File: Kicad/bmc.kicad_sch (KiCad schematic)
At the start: 30 parts, among them J1601 Header, J1602 Header, J1603 Conn_01x05, J1604 Double-mini-DIN-6, SW1601 SW_DIP_x01, SW1602 SW_DIP_x01, U1601 STM32F031K6T6

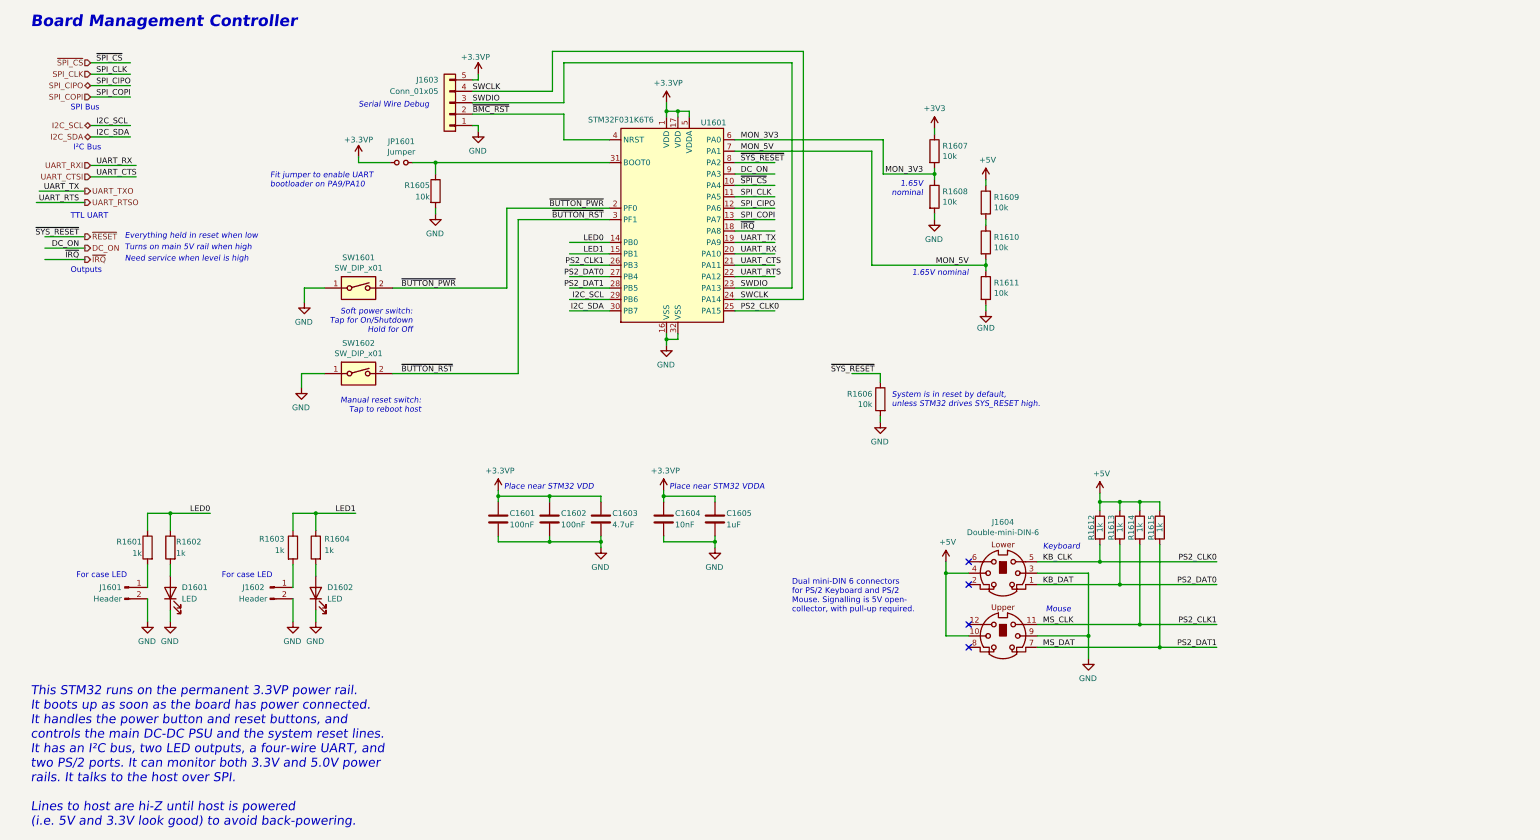
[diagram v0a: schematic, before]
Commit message: Update schematic files to Kicad 6.
Had to fix some symbols which didn't have perfect matches in K6.
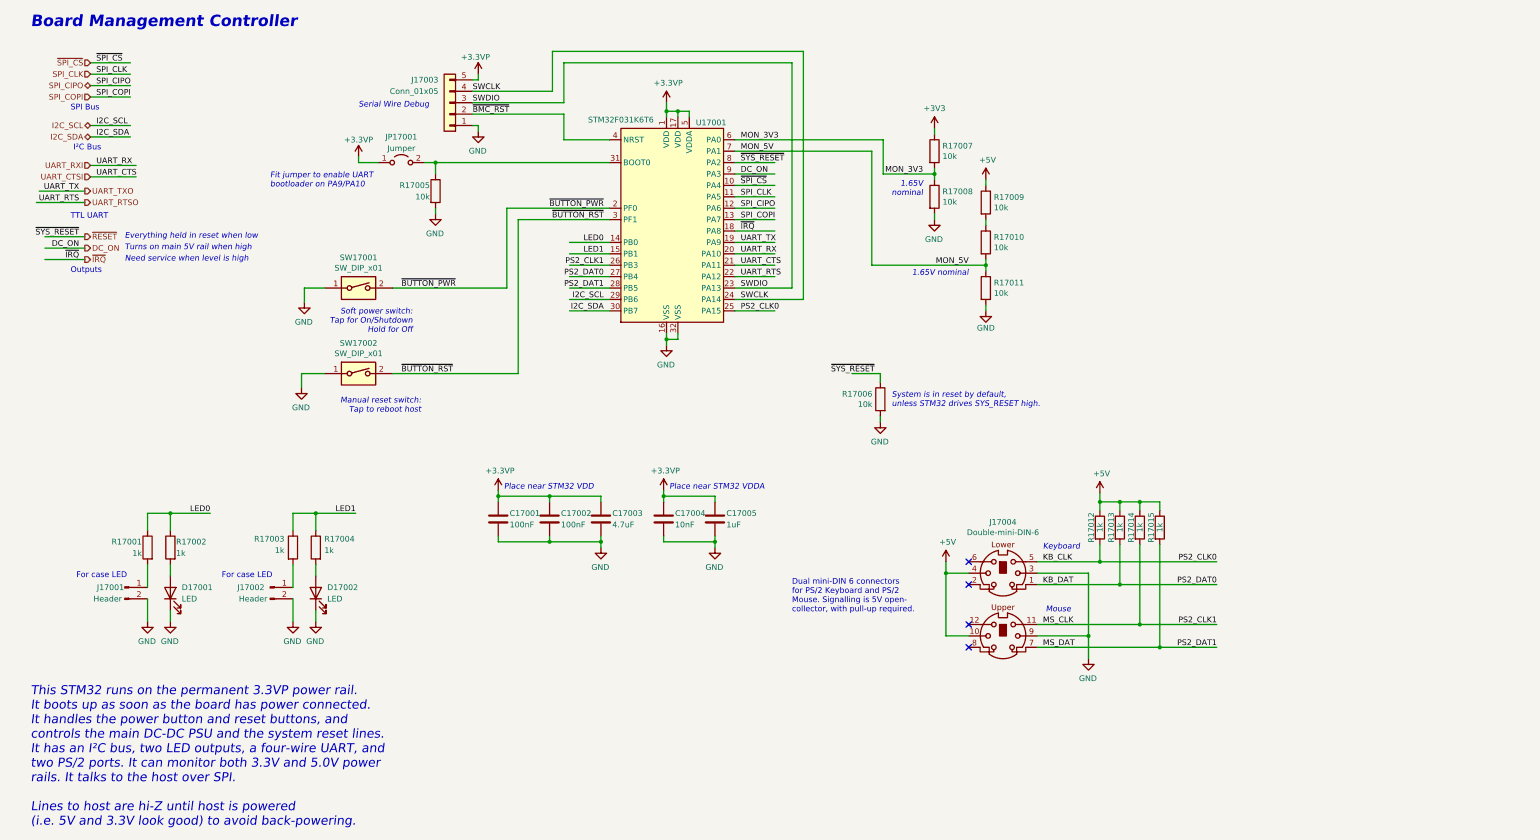
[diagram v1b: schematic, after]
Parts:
- JP17001: renamed from JP1601; symbol Neotron-Common-Hardware-rescue:Jumper_NO_Small-Device -> Jumper:Jumper_2_Open
- renumbered C1601 to C17001, C1602 to C17002, C1603 to C17003, C1604 to C17004, C1605 to C17005, D1601 to D17001, D1602 to D17002, J1601 to J17001, J1602 to J17002, J1603 to J17003, J1604 to J17004, R1601 to R17001, R1602 to R17002, R1603 to R17003, R1604 to R17004, R1605 to R17005, R1606 to R17006, R1607 to R17007, R1608 to R17008, R1609 to R17009, R1610 to R17010, R1611 to R17011, R1612 to R17012, R1613 to R17013, R1614 to R17014, R1615 to R17015, SW1601 to SW17001, SW1602 to SW17002, U1601 to U17001

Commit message: Imported sheets from Neotron Pico.
Standardised on +3V3 not +3.3V
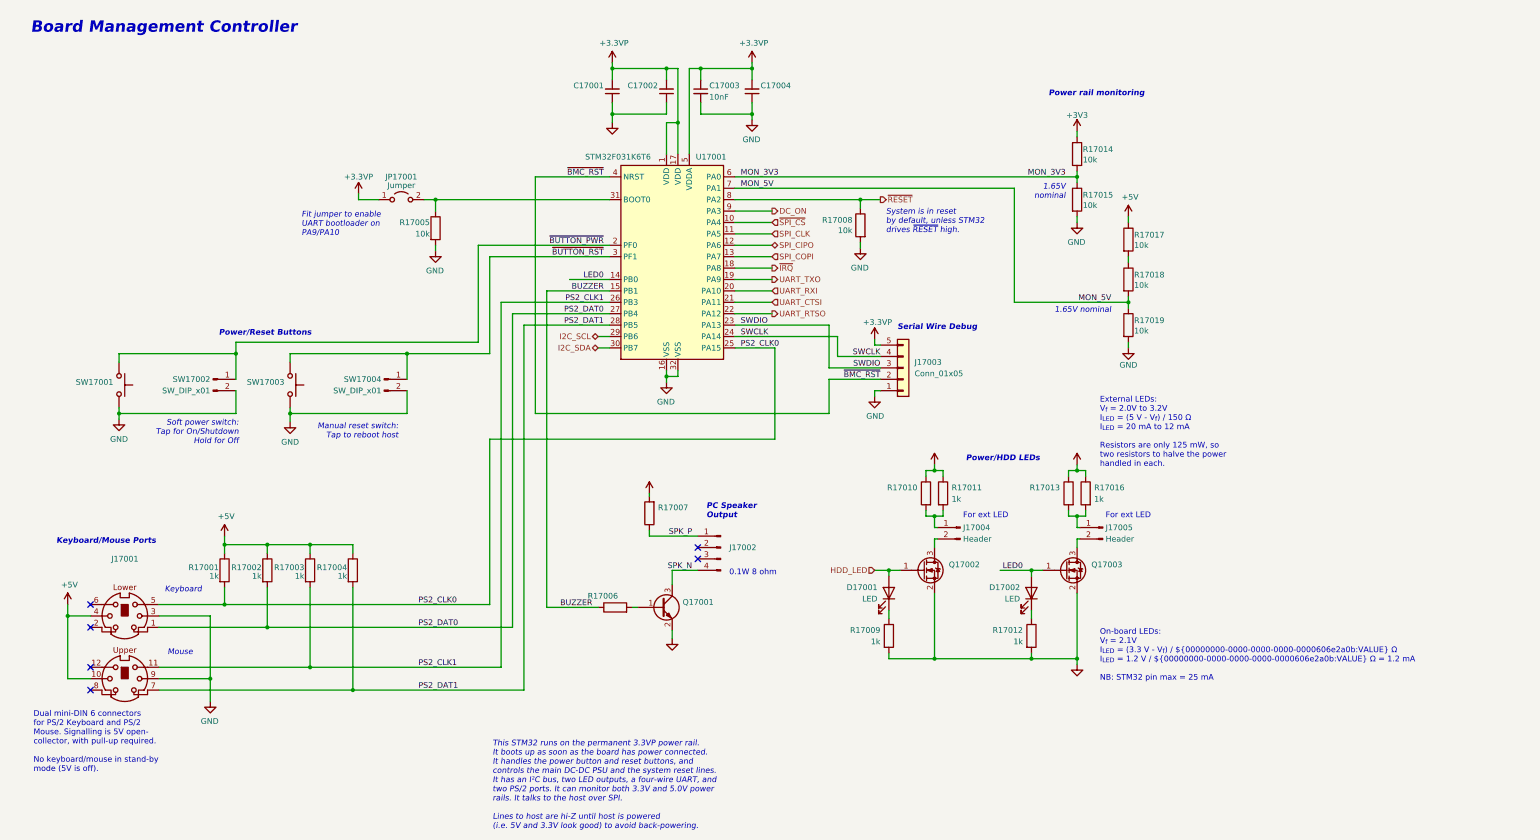
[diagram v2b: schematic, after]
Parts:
- removed C17001, C17002: 100nF, Capacitor_SMD:C_0805_2012Metric_Pad1.18x1.45mm_HandSolder, symbol Device:C
- removed C17003: 4.7uF, Capacitor_SMD:C_0805_2012Metric_Pad1.18x1.45mm_HandSolder, symbol Device:C
- removed C17005: 1uF, Capacitor_SMD:C_0805_2012Metric_Pad1.18x1.45mm_HandSolder, symbol Device:C
- removed J17004: Double-mini-DIN-6, Neotron-Common-Hardware:Double_mini-DIN_6, symbol Neotron-Common-Hardware:Double-mini-DIN-6
- added C17001, C17002, C17004: (no value), symbol Device:C_Small
- added J17001: (no value), symbol Neotron-Common-Hardware:Double-mini-DIN-6
- added J17002: (no value), symbol Connector:Conn_01x04_Male
- added Q17001: (no value), symbol Transistor_BJT:BC817
- added Q17002, Q17003: (no value), symbol Transistor_FET:2N7002
- added R17006, R17007, R17010, R17013: (no value), symbol Device:R
- added SW17001, SW17003: (no value), symbol Switch:SW_Push
- C17003: renamed from C17004; symbol Device:C -> Device:C_Small; Digikey 1276-1249-1-ND -> (none); JLCPCB Collection (none) -> Basic; Tolerance X5R -> X7R; Voltage 10V -> 50V
- D17001, D17002: JLCPCB Collection (none) -> Basic; LCSC Part# (none) -> C2296; MPN CPL-LED-3MM-RED -> 17-21SUYC/TR8; Manufacturer CPL -> Hubei KENTO; Voltage (none) -> 2.1V
- J17003, JP17001: DNP 1 -> 0
- J17004: renamed from J17001; DNP 1 -> 0
- J17005: renamed from J17002; DNP 1 -> 0
- R17001: renamed from R17012; JLCPCB Collection (none) -> Basic; MPN CPL-RES-0805-1K-0.125W -> 0805W8F1001T5E; Manufacturer CPL -> Uniroyal
- R17002: renamed from R17013; JLCPCB Collection (none) -> Basic; MPN CPL-RES-0805-1K-0.125W -> 0805W8F1001T5E; Manufacturer CPL -> Uniroyal
- R17003: renamed from R17014; JLCPCB Collection (none) -> Basic; MPN CPL-RES-0805-1K-0.125W -> 0805W8F1001T5E; Manufacturer CPL -> Uniroyal
- R17004: renamed from R17015; JLCPCB Collection (none) -> Basic; MPN CPL-RES-0805-1K-0.125W -> 0805W8F1001T5E; Manufacturer CPL -> Uniroyal
- R17005: JLCPCB Collection (none) -> Basic; MPN CPL-RES-0805-10K-0.125W -> 0805W8F1002T5E; Manufacturer CPL -> Uniroyal
- R17008: renamed from R17006; JLCPCB Collection (none) -> Basic; MPN CPL-RES-0805-10K-0.125W -> 0805W8F1002T5E; Manufacturer CPL -> Uniroyal
- R17009: renamed from R17002; JLCPCB Collection (none) -> Basic; MPN CPL-RES-0805-1K-0.125W -> 0805W8F1001T5E; Manufacturer CPL -> Uniroyal
- R17011: renamed from R17001; JLCPCB Collection (none) -> Basic; MPN CPL-RES-0805-1K-0.125W -> 0805W8F1001T5E; Manufacturer CPL -> Uniroyal
- R17012: renamed from R17004; JLCPCB Collection (none) -> Basic; MPN CPL-RES-0805-1K-0.125W -> 0805W8F1001T5E; Manufacturer CPL -> Uniroyal
- R17014: renamed from R17007; JLCPCB Collection (none) -> Basic; MPN CPL-RES-0805-10K-0.125W -> 0805W8F1002T5E; Manufacturer CPL -> Uniroyal
- R17015: renamed from R17008; JLCPCB Collection (none) -> Basic; MPN CPL-RES-0805-10K-0.125W -> 0805W8F1002T5E; Manufacturer CPL -> Uniroyal
- R17016: renamed from R17003; JLCPCB Collection (none) -> Basic; MPN CPL-RES-0805-1K-0.125W -> 0805W8F1001T5E; Manufacturer CPL -> Uniroyal
- R17017: renamed from R17009; JLCPCB Collection (none) -> Basic; MPN CPL-RES-0805-10K-0.125W -> 0805W8F1002T5E; Manufacturer CPL -> Uniroyal
- R17018: renamed from R17010; JLCPCB Collection (none) -> Basic; MPN CPL-RES-0805-10K-0.125W -> 0805W8F1002T5E; Manufacturer CPL -> Uniroyal
- R17019: renamed from R17011; JLCPCB Collection (none) -> Basic; MPN CPL-RES-0805-10K-0.125W -> 0805W8F1002T5E; Manufacturer CPL -> Uniroyal
- SW17002: renamed from SW17001; symbol Switch:SW_DIP_x01 -> Connector:Conn_01x02_Male; DNP 1 -> 0
- SW17004: renamed from SW17002; symbol Switch:SW_DIP_x01 -> Connector:Conn_01x02_Male; DNP 1 -> 0
- U17001: symbol MCU_ST_STM32F0:STM32F031K6Tx -> MCU_ST_STM32F0:STM32F030K6Tx; Digikey 497-17341-ND -> (none); JLCPCB Collection (none) -> Extended; LCSC Part# C526904 -> C46830; MPN STM32F031K6T6 -> STM32F030K6T6; Manufacturer ST Micro -> ST; Mouser 511-STM32F031K6T6 -> (none)
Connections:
- net +3.3VP: now also C17001.2, C17002.2, C17004.2
- net +5V: now also R17011.1, R17016.1, J17001.10, J17001.4, R17007.2, R17010.1, R17013.1
- net GND: now also R17009.2, R17012.2, SW17002.2 (Pin_2), SW17004.2 (Pin_2), C17001.1, C17002.1, C17004.1, J17001.3, J17001.9, Q17001.2 (E), Q17002.2 (S), Q17003.2 (S), SW17001.1, SW17003.1; no longer D17001.1 (K), D17002.1 (K), J17004.2 (Pin_2), J17005.2 (Pin_2), SW17002.1, SW17004.1
- net LED0: now also D17002.2 (A), Q17003.1 (G); no longer R17009.1, R17011.1
- net ~{BUTTON_PWR}: now also SW17002.1 (Pin_1), SW17001.2; no longer SW17002.2
- net ~{BUTTON_RST}: now also SW17004.1 (Pin_1), SW17003.2; no longer SW17004.2
- net HDD_LED: now reaches D17001.2 (A)
- net HDD_LED: now also Q17002.1 (G); no longer R17009.2
- net at J17004.1 (Pin_1), R17011.2: now also R17010.2
- net at J17005.1 (Pin_1), R17016.2: now also R17013.2
- net KB_CLK renamed PS2_CLK0
- net PS2_CLK0: now also J17001.5
- net KB_DAT renamed PS2_DAT0
- net PS2_DAT0: now also J17001.1
- removed net LED1: R17012.1, R17016.1, U17001.15 (PB1)
- net MS_CLK renamed PS2_CLK1
- net PS2_CLK1: now also J17001.11
- net MS_DAT renamed PS2_DAT1
- net PS2_DAT1: now also J17001.7
- new net: D17001.1 (K), R17009.1
- new net: J17004.2 (Pin_2), Q17002.3 (D)
- new net: D17002.1 (K), R17012.1
- new net: J17005.2 (Pin_2), Q17003.3 (D)
- new net: Q17001.1 (B), R17006.2
- new net BUZZER: R17006.1, U17001.15 (PB1)
- new net SPK_N: J17002.4 (Pin_4), Q17001.3 (C)
- new net SPK_P: J17002.1 (Pin_1), R17007.1
- no-connect marks 4 -> 6
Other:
- note added: "0.1W 8 ohm"
- note added: "Dual mini-DIN 6 connectors for PS/2 Keyboard and PS/2 Mouse. Signalling is 5V open- collector, with pull-up required. No keyboard/mouse in stand-by mode (5V is off)."
- note added: "External LEDs: V_{f} = 2.0V to 3.2V I_{LED} = (5 V - V_{f}) / 150 Ω I_{LED} = 20 mA to 12 mA Resistors are only 125 mW, so two resistors to halve the power handled in each."
- note added: "For ext LED"
- note added: "Keyboard/Mouse Ports"
- note added: "On-board LEDs: V_{f} = 2.1V I_{LED} = (3.3 V - V_{f}) / ${00000000-0000-0000-0000-0000606e2a0b:VALUE} Ω I_{LED} = 1.2 V / ${00000000-0000-0000-0000-0000606e2a0b:VALUE} Ω = 1.2 mA NB: STM32 pin max = 25 mA"
- note added: "PC Speaker Output"
- note added: "Power rail monitoring"
- note added: "Power/HDD LEDs"
- note added: "Power/Reset Buttons"
- note added: "System is in reset by default, unless STM32 drives ~{RESET} high."
- note removed: "Dual mini-DIN 6 connectors for PS/2 Keyboard and PS/2 Mouse. Signalling is 5V open- collector, with pull-up required."
- note removed: "Everything held in reset when low"
- note removed: "For case LED"
- note removed: "I²C Bus"
- note removed: "Need service when level is high"
- note removed: "Outputs"
- note removed: "Place near STM32 VDD"
- note removed: "Place near STM32 VDDA"
- note removed: "SPI Bus"
- note removed: "System is in reset by default, unless STM32 drives SYS_RESET high."
- note removed: "TTL UART"
- note removed: "Turns on main 5V rail when high"
- company: https://neotron-compute.github.io/ -> https://neotron-compute.github.io
- moved on the sheet: C17003, D17001, D17002, J17003, J17004, J17005, JP17001, R17001, R17002, R17003, R17004, R17005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

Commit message: Set missing footprints and update PCB
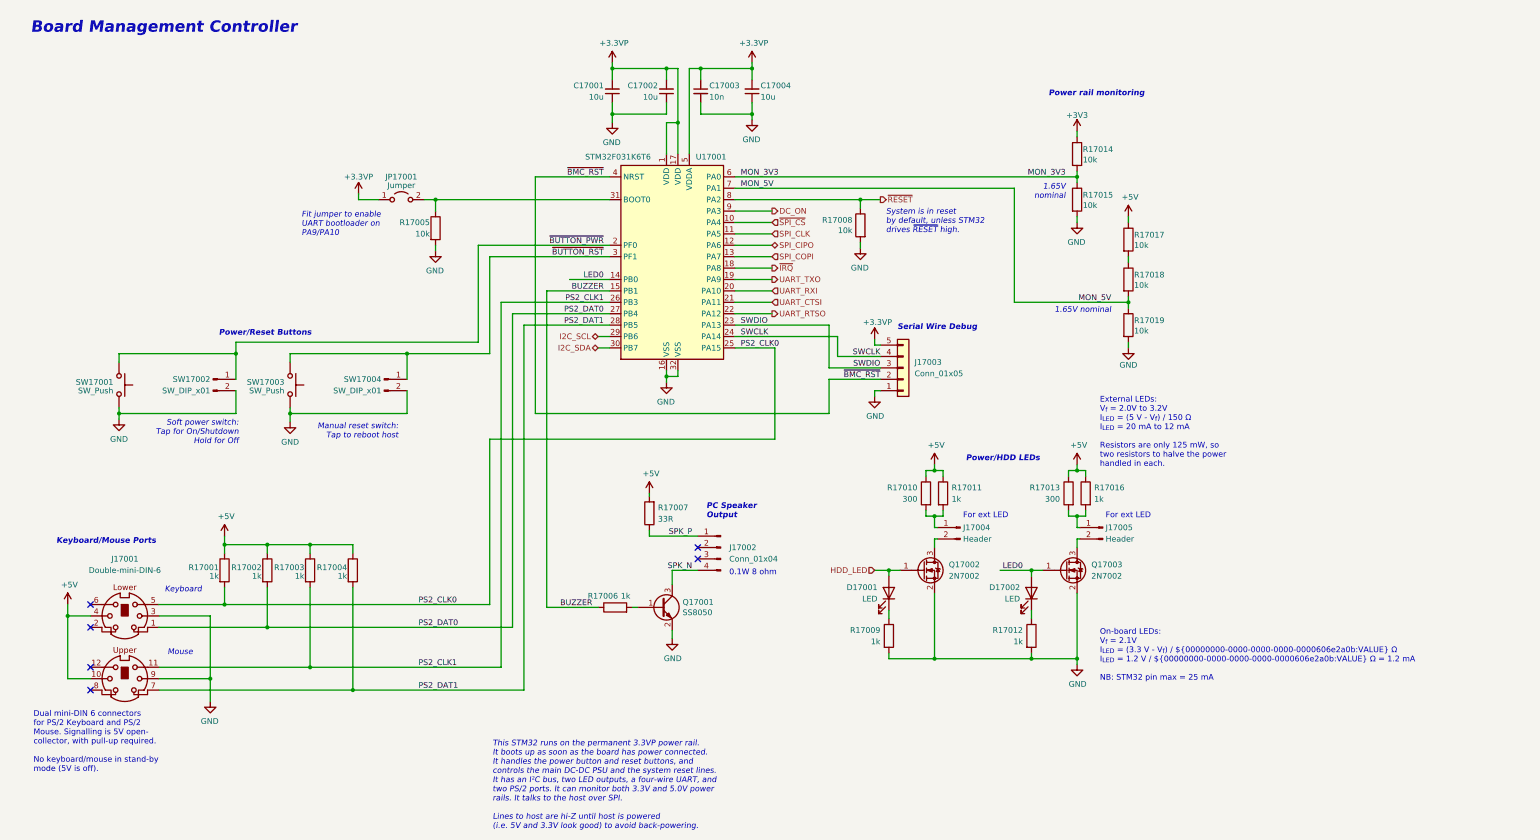
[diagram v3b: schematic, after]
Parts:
- C17001, C17002, C17004: value (none) -> 10u; footprint (none) -> Capacitor_SMD:C_0805_2012Metric_Pad1.18x1.45mm_HandSolder; JLCPCB Collection Basic -> (none); LCSC Part# C15850 -> (none); MPN CL21A106KAYNNNE -> (none); Manufacturer Samsung -> (none)
- C17003: value 10nF -> 10n
- D17001, D17002: footprint LED_THT:LED_D3.0mm -> LED_SMD:LED_0805_2012Metric
- J17001: value (none) -> Double-mini-DIN-6; footprint (none) -> Neotron-Common-Hardware:Double_mini-DIN_6
- J17002: value (none) -> Conn_01x04; footprint (none) -> Connector_PinHeader_2.54mm:PinHeader_1x04_P2.54mm_Vertical
- Q17001: value (none) -> SS8050; footprint (none) -> Package_TO_SOT_SMD:SOT-23
- Q17002, Q17003: value (none) -> 2N7002; footprint (none) -> Package_TO_SOT_SMD:SOT-23
- R17006: value (none) -> 1k; footprint (none) -> Resistor_SMD:R_0805_2012Metric_Pad1.20x1.40mm_HandSolder
- R17007: value (none) -> 33R; footprint (none) -> Resistor_SMD:R_0805_2012Metric_Pad1.20x1.40mm_HandSolder
- R17010, R17013: value (none) -> 300; footprint (none) -> Resistor_SMD:R_0805_2012Metric_Pad1.20x1.40mm_HandSolder
- SW17001, SW17003: value (none) -> SW_Push; footprint (none) -> Button_Switch_THT:SW_PUSH_6mm

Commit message: Re-imported from Neotron Pico v1.1.
This time I deleted the sheets from the top level and then re-added pointing at the new files. I also reset the PCB dimensions to match the Neotron Pico.

This seems to have done a better job importing footprints.
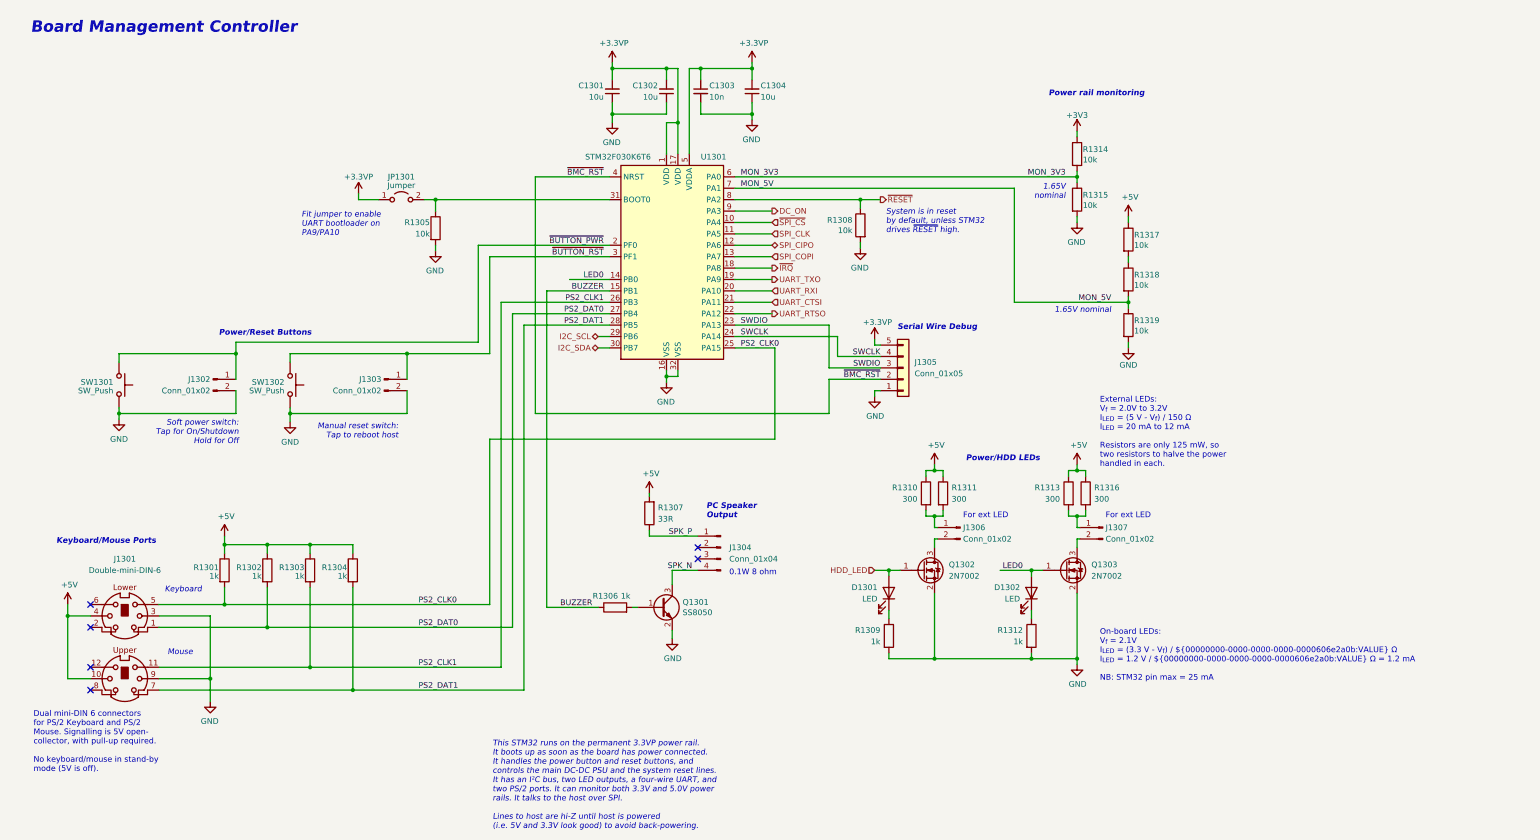
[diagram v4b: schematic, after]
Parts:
- C1301: renamed from C17001; JLCPCB Collection (none) -> Basic; LCSC Part# (none) -> C15850; MPN (none) -> CL21A106KAYNNNE; Manufacturer (none) -> Samsung
- C1302: renamed from C17002; JLCPCB Collection (none) -> Basic; LCSC Part# (none) -> C15850; MPN (none) -> CL21A106KAYNNNE; Manufacturer (none) -> Samsung
- C1304: renamed from C17004; JLCPCB Collection (none) -> Basic; LCSC Part# (none) -> C15850; MPN (none) -> CL21A106KAYNNNE; Manufacturer (none) -> Samsung
- D1301: renamed from D17001; footprint LED_SMD:LED_0805_2012Metric -> LED_SMD:LED_0805_2012Metric_Pad1.15x1.40mm_HandSolder
- D1302: renamed from D17002; footprint LED_SMD:LED_0805_2012Metric -> LED_SMD:LED_0805_2012Metric_Pad1.15x1.40mm_HandSolder
- J1302: renamed from SW17002; value SW_DIP_x01 -> Conn_01x02
- J1303: renamed from SW17004; value SW_DIP_x01 -> Conn_01x02
- J1306: renamed from J17004; value Header -> Conn_01x02
- J1307: renamed from J17005; value Header -> Conn_01x02
- R1311: renamed from R17011; value 1k -> 300; LCSC Part# C17513 -> C17617; MPN 0805W8F1001T5E -> 0805W8F3000T5E
- R1316: renamed from R17016; value 1k -> 300; LCSC Part# C17513 -> C17617; MPN 0805W8F1001T5E -> 0805W8F3000T5E
- U1301: renamed from U17001; value STM32F031K6T6 -> STM32F030K6T6
- renumbered C17003 to C1303, J17001 to J1301, J17002 to J1304, J17003 to J1305, JP17001 to JP1301, Q17001 to Q1301, Q17002 to Q1302, Q17003 to Q1303, R17001 to R1301, R17002 to R1302, R17003 to R1303, R17004 to R1304, R17005 to R1305, R17006 to R1306, R17007 to R1307, R17008 to R1308, R17009 to R1309, R17010 to R1310, R17012 to R1312, R17013 to R1313, R17014 to R1314, R17015 to R1315, R17017 to R1317, R17018 to R1318, R17019 to R1319, SW17001 to SW1301, SW17003 to SW1302
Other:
- company: https://neotron-compute.github.io -> https://neotron-compute.github.io/
